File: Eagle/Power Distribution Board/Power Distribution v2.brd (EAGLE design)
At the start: 110 x 60 mm, 43 parts, among them IC1 INA138, IC2 INA138, IC3 INA138

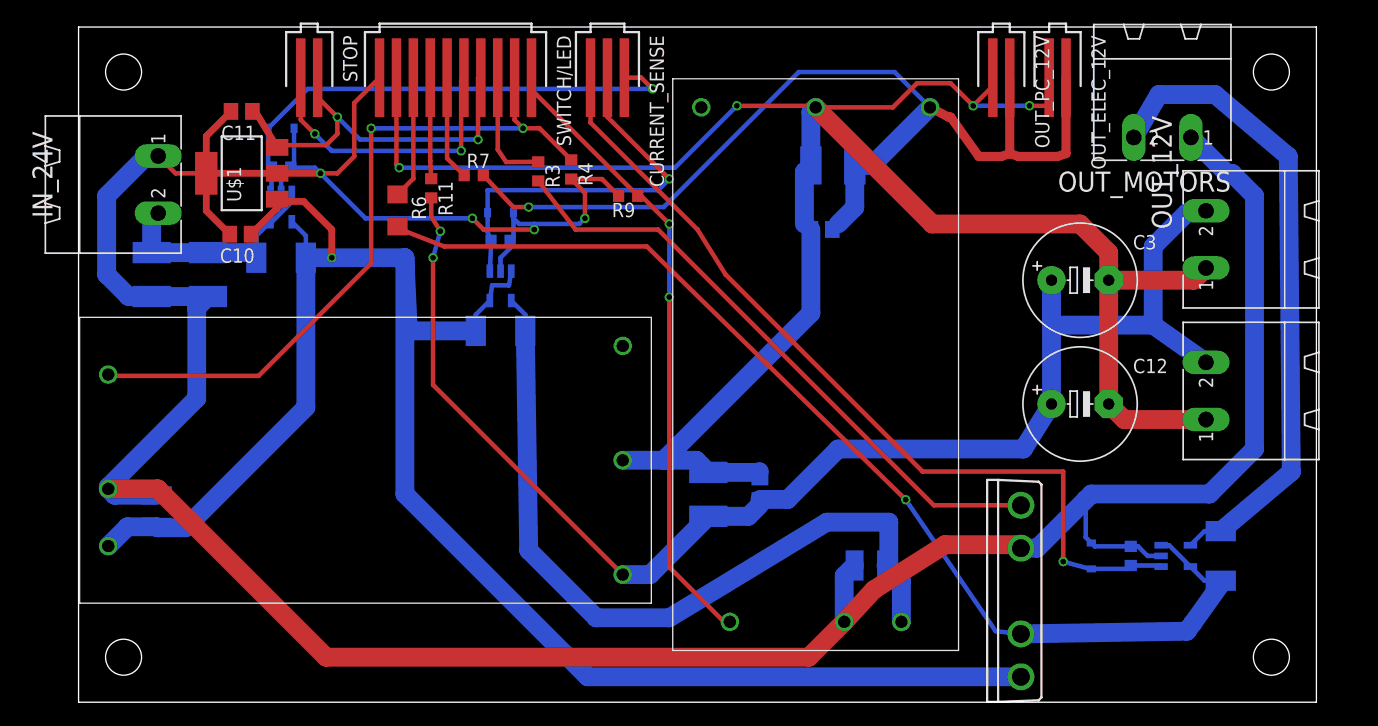
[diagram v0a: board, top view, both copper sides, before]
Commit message: Reorganise projects & cleanup
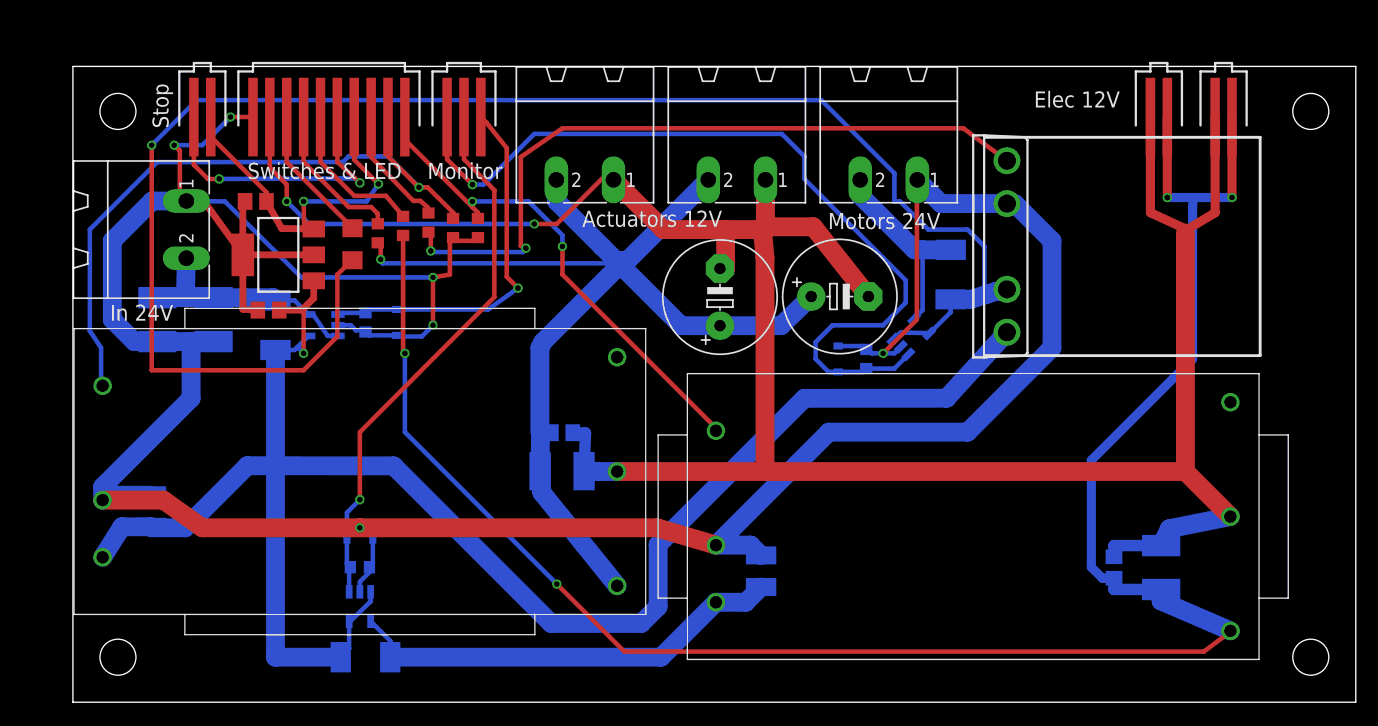
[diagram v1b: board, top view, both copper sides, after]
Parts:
- TRACO_ELEC: value TEN-30 -> TEN-3030W
- TRACO_SERVO: device custom:TRACO2X1 -> custom:TRACO2X1_50W
- moved OUT_12V 61.2 mm to (43.0, 51.5), turned to 180 degrees
- moved OUT_12V_SERVO 52.5 mm to (56.5, 51.5), turned to 180 degrees
- moved C5 46.1 mm to (94.2, 12.0), turned to 90 degrees
- moved C6 39.7 mm to (90.0, 12.0), turned to 90 degrees
- moved R10 34.7 mm to (75.5, 38.0)
- moved C3 32.0 mm to (55.0, 36.0), turned to 90 degrees
- moved R8 31.6 mm to (23.0, 12.0)
- moved U$3 31.6 mm to (23.0, 14.5)
- moved R5 31.4 mm to (23.5, 4.00)
- moved IC2 31.1 mm to (23.0, 8.50)
- moved MOTOR_RELAY 30.6 mm to (80.5, 40.5)
- moved IC3 30.5 mm to (72.0, 32.5), turned to 45 degrees
- moved R12 29.3 mm to (68.0, 30.5)
- moved U$4 28.5 mm to (65.5, 30.5)
- moved OUT_MOTORS 24.6 mm to (70.0, 51.5)
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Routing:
- net 12V_ELEC: track 90.3 -> 171.6 mm, vias 1 -> 4
- net 12V_MOTORS: track 98.0 -> 144.4 mm
- net N$5: track 57.4 -> 17.8 mm
- net AGND: track 189.5 -> 219.4 mm, vias 4 -> 2
- net N$7: track 69.1 -> 39.5 mm
- net 12V_SERVO: track 128.8 -> 101.3 mm, vias 2 -> 1
- net GND: track 301.3 -> 281.6 mm, vias 4 -> 6
- net ELEC_CURRENT: track 35.1 -> 48.9 mm
- net ELEC_ONOFF: track 56.1 -> 44.4 mm
- net IN_CURRENT: track 44.4 -> 33.2 mm
- net N$12: track 55.2 -> 63.8 mm, vias 0 -> 2
- net 24VIN: track 163.6 -> 157.4 mm
- net SERVO_LED: track 8.98 -> 13.4 mm
- net SERVO_ONOFF: track 63.3 -> 59.2 mm, vias 2 -> 1
- net ELEC_LED: track 9.30 -> 13.4 mm
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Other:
- board size 110 x 60 mm -> 114 x 56.5 mm
- board text added: "Actuators 12V"
- board text added: "Elec 12V"
- board text added: "In 24V"
- board text added: "Monitor"
- board text added: "Motors 24V"
- board text added: "Stop"
- board text added: "Switches & LED"
